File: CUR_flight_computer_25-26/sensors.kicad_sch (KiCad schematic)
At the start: 25 parts, among them U2 IIS2MDC, U3 LPS22HB, U4 LSM6DSV80X

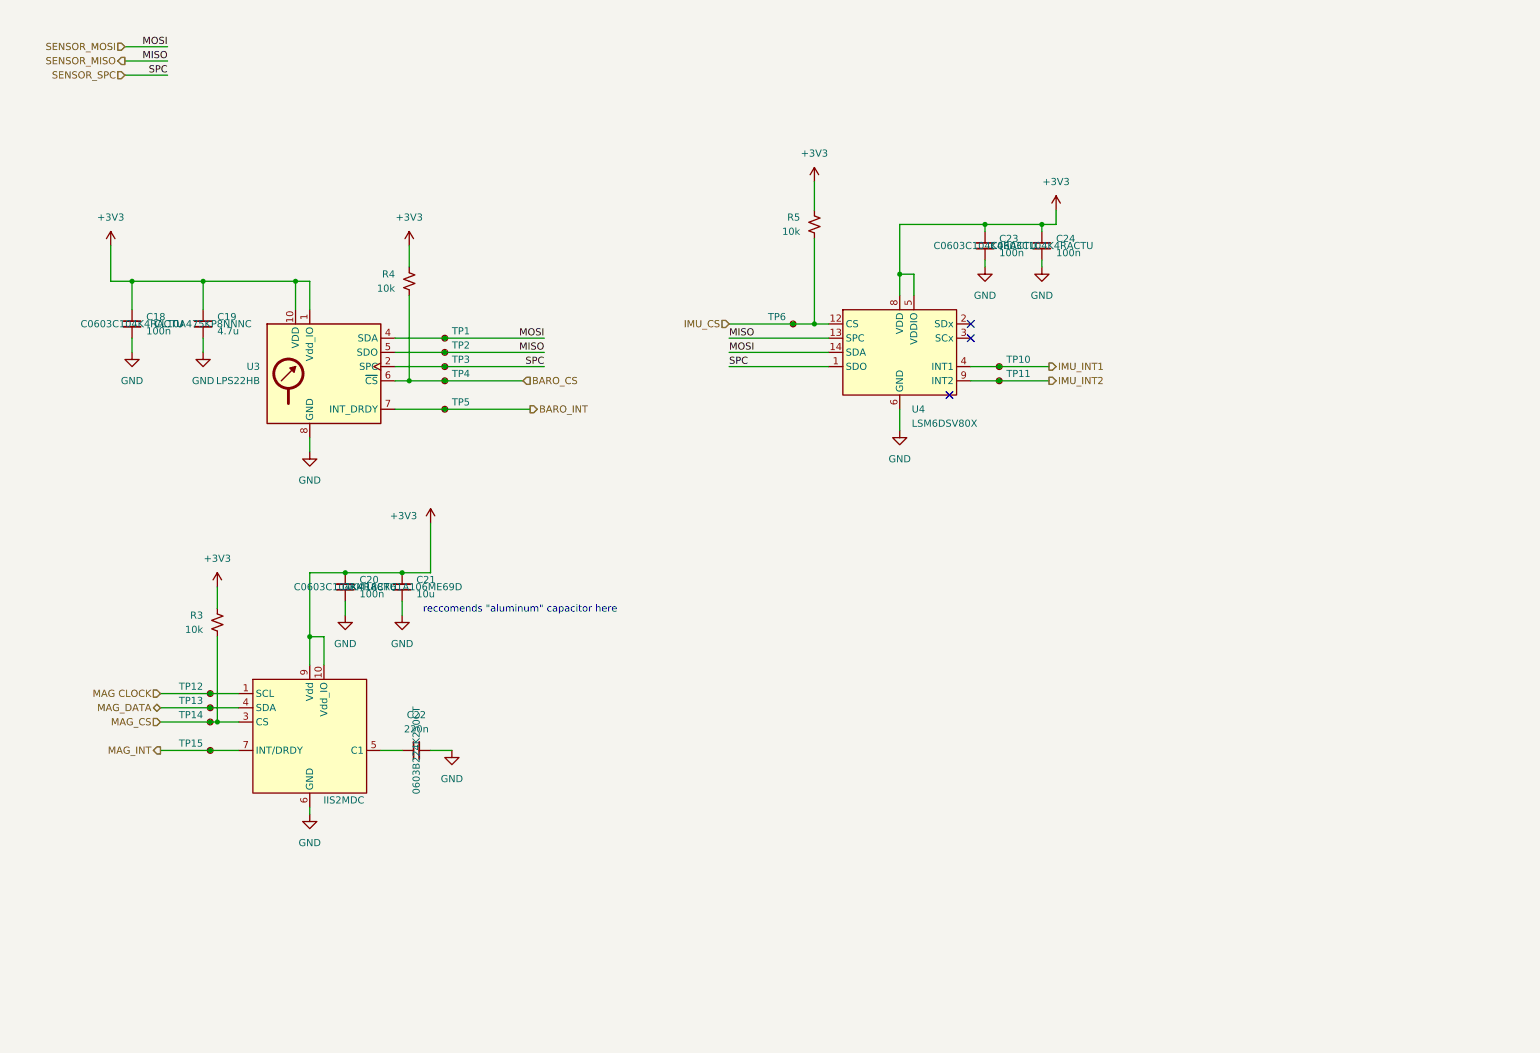
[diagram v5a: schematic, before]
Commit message: Add MPNs for ICs
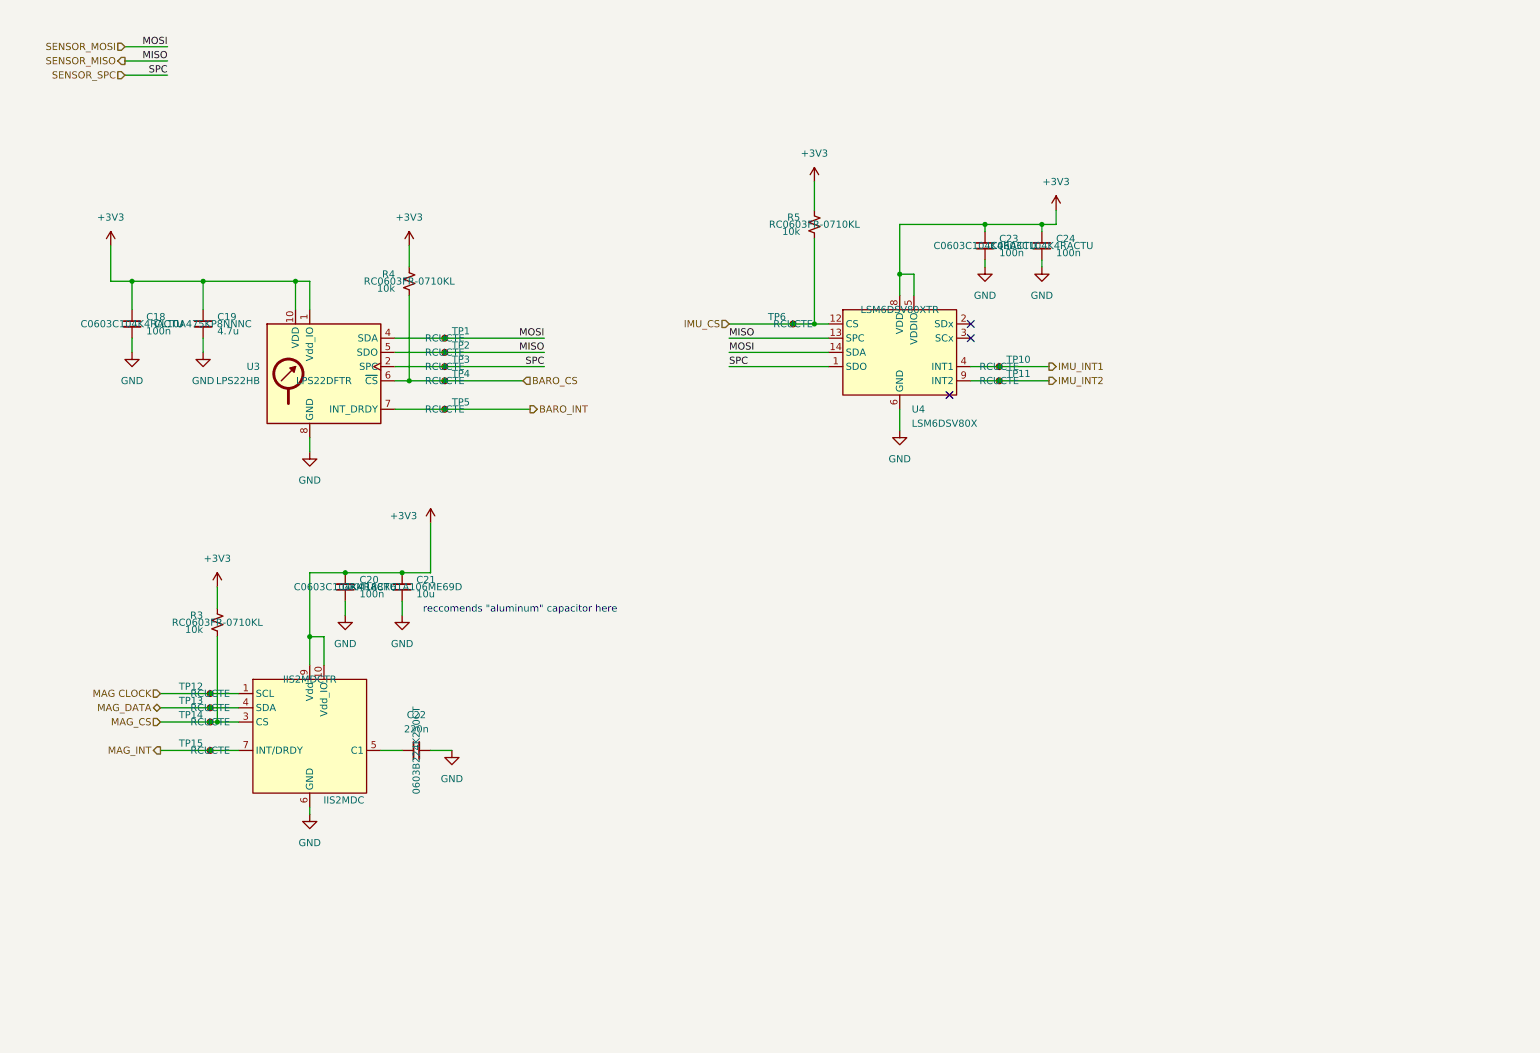
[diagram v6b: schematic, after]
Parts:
- R3, R4, R5: MPN (none) -> RC0603FR-0710KL
- TP1, TP10, TP11, TP12, TP13, TP14, TP15, TP2, TP3, TP4, TP5, TP6: value TestPoint_Small -> RCUCTE; MPN (none) -> RCUCTE
- U2: MPN (none) -> IIS2MDCTR
- U3: MPN (none) -> LPS22DFTR
- U4: MPN (none) -> LSM6DSV80XTR
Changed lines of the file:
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@@
+			)
+		)
+		(property "MPN" "RC0603FR-0710KL"
+			(at 156.21 50.8 0)
+			(effects
+				(font
+					(size 1.27 1.27)
+				)
 			)
 		)
@@
 			)
 		)
-		(property "Value" "TestPoint_Small"
+		(property "Value" "RCUCTE"
 			(at 91.44 77.4699 0)
 			(effects
@@
 				)
 				(hide yes)
+			)
+		)
+		(property "MPN" "RCUCTE"
+			(at 90.17 76.2 0)
+			(effects
+				(font
+					(size 1.27 1.27)
+				)
 			)
 		)
@@
 			)
 		)
-		(property "Value" "TestPoint_Small"
+		(property "Value" "RCUCTE"
 			(at 153.162 65.024 0)
 			(effects
@@
 			)
 		)
+		(property "MPN" "RCUCTE"
+			(at 152.4 68.58 0)
+			(effects
+				(font
+					(size 1.27 1.27)
+				)
+			)
+		)
 		(pin "1"
 		)
@@
 			)
 		)
+		(property "MPN" "LPS22DFTR"
+			(at 68.58 78.74 0)
+			(effects
+				(font
+					(size 1.27 1.27)
+				)
+			)
+		)
 		(pin "7"
 		)
@@
 			)
 		)
+		(property "MPN" "RC0603FR-0710KL"
+			(at 83.82 60.96 0)
+			(effects
+				(font
+					(size 1.27 1.27)
+				)
+			)
+		)
 		(pin "1"
 		)
@@
 			)
 		)
-		(property "Value" "TestPoint_Small"
+		(property "Value" "RCUCTE"
 			(at 89.408 67.564 0)
 			(effects
@@
 			)
 		)
+		(property "MPN" "RCUCTE"
+			(at 90.17 71.12 0)
+			(effects
+				(font
+					(size 1.27 1.27)
+				)
+			)
+		)
 		(pin "1"
 		)
@@
 			)
 		)
+		(property "MPN" "LSM6DSV80XTR"
+			(at 171.45 66.04 0)
+			(effects
+				(font
+					(size 1.27 1.27)
+				)
+			)
+		)
 		(pin "7"
 		)
@@
 			)
 		)
-		(property "Value" "TestPoint_Small"
+		(property "Value" "RCUCTE"
 			(at 91.44 74.9299 0)
 			(effects
@@
 			)
 		)
+		(property "MPN" "RCUCTE"
+			(at 90.17 73.66 0)
+			(effects
+				(font
+					(size 1.27 1.27)
+				)
+			)
+		)
 		(pin "1"
 		)
@@
 			)
 		)
-		(property "Value" "TestPoint_Small"
+		(property "Value" "RCUCTE"
 			(at 91.44 85.0899 0)
 			(effects
@@
 				)
 				(hide yes)
+			)
+		)
+		(property "MPN" "RCUCTE"
+			(at 90.17 83.82 0)
+			(effects
+				(font
+					(size 1.27 1.27)
+				)
 			)
 		)
@@
 			)
 		)
-		(property "Value" "TestPoint_Small"
+		(property "Value" "RCUCTE"
 			(at 46.99 146.0499 0)
 			(effects
@@
 			)
 		)
+		(property "MPN" "RCUCTE"
+			(at 48.26 144.78 0)
+			(effects
+				(font
+					(size 1.27 1.27)
+				)
+			)
+		)
 		(pin "1"
 		)
@@
 			)
 		)
+		(property "MPN" "IIS2MDCTR"
+			(at 66.04 132.08 0)
+			(effects
+				(font
+					(size 1.27 1.27)
+				)
+			)
+		)
 		(pin "4"
 		)
@@
 			)
 		)
-		(property "Value" "TestPoint_Small"
+		(property "Value" "RCUCTE"
 			(at 190.5 80.0099 0)
 			(effects
@@
 				)
 				(hide yes)
+			)
+		)
+		(property "MPN" "RCUCTE"
+			(at 189.23 78.74 0)
+			(effects
+				(font
+					(size 1.27 1.27)
+				)
 			)
 		)
@@
 			)
 		)
-		(property "Value" "TestPoint_Small"
+		(property "Value" "RCUCTE"
 			(at 49.022 131.064 0)
 			(effects
@@
 			)
 		)
+		(property "MPN" "RCUCTE"
+			(at 48.26 134.62 0)
+			(effects
+				(font
+					(size 1.27 1.27)
+				)
+			)
+		)
 		(pin "1"
 		)
@@
 				)
 				(hide yes)
+			)
+		)
+		(property "MPN" "RC0603FR-0710KL"
+			(at 49.53 121.92 0)
+			(effects
+				(font
+					(size 1.27 1.27)
+				)
 			)
 		)
@@
 			)
 		)
-		(property "Value" "TestPoint_Small"
+		(property "Value" "RCUCTE"
 			(at 46.99 138.4299 0)
 			(effects
@@
 			)
 		)
+		(property "MPN" "RCUCTE"
+			(at 48.26 137.16 0)
+			(effects
+				(font
+					(size 1.27 1.27)
+				)
+			)
+		)
 		(pin "1"
 		)
@@
 			)
 		)
-		(property "Value" "TestPoint_Small"
+		(property "Value" "RCUCTE"
 			(at 188.468 72.644 0)
 			(effects
@@
 			)
 		)
+		(property "MPN" "RCUCTE"
+			(at 189.23 76.2 0)
+			(effects
+				(font
+					(size 1.27 1.27)
+				)
+			)
+		)
 		(pin "1"
 		)
@@
 			)
 		)
-		(property "Value" "TestPoint_Small"
+		(property "Value" "RCUCTE"
 			(at 91.44 80.0099 0)
 			(effects
@@
 				)
 				(hide yes)
+			)
+		)
+		(property "MPN" "RCUCTE"
+			(at 90.17 78.74 0)
+			(effects
+				(font
+					(size 1.27 1.27)
+				)
 			)
 		)
@@
 			)
 		)
-		(property "Value" "TestPoint_Small"
+		(property "Value" "RCUCTE"
 			(at 46.99 140.9699 0)
 			(effects
@@
 			)
 		)
+		(property "MPN" "RCUCTE"
+			(at 48.26 139.7 0)
+			(effects
+				(font
+					(size 1.27 1.27)
+				)
+			)
+		)

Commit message: Hide MPNs
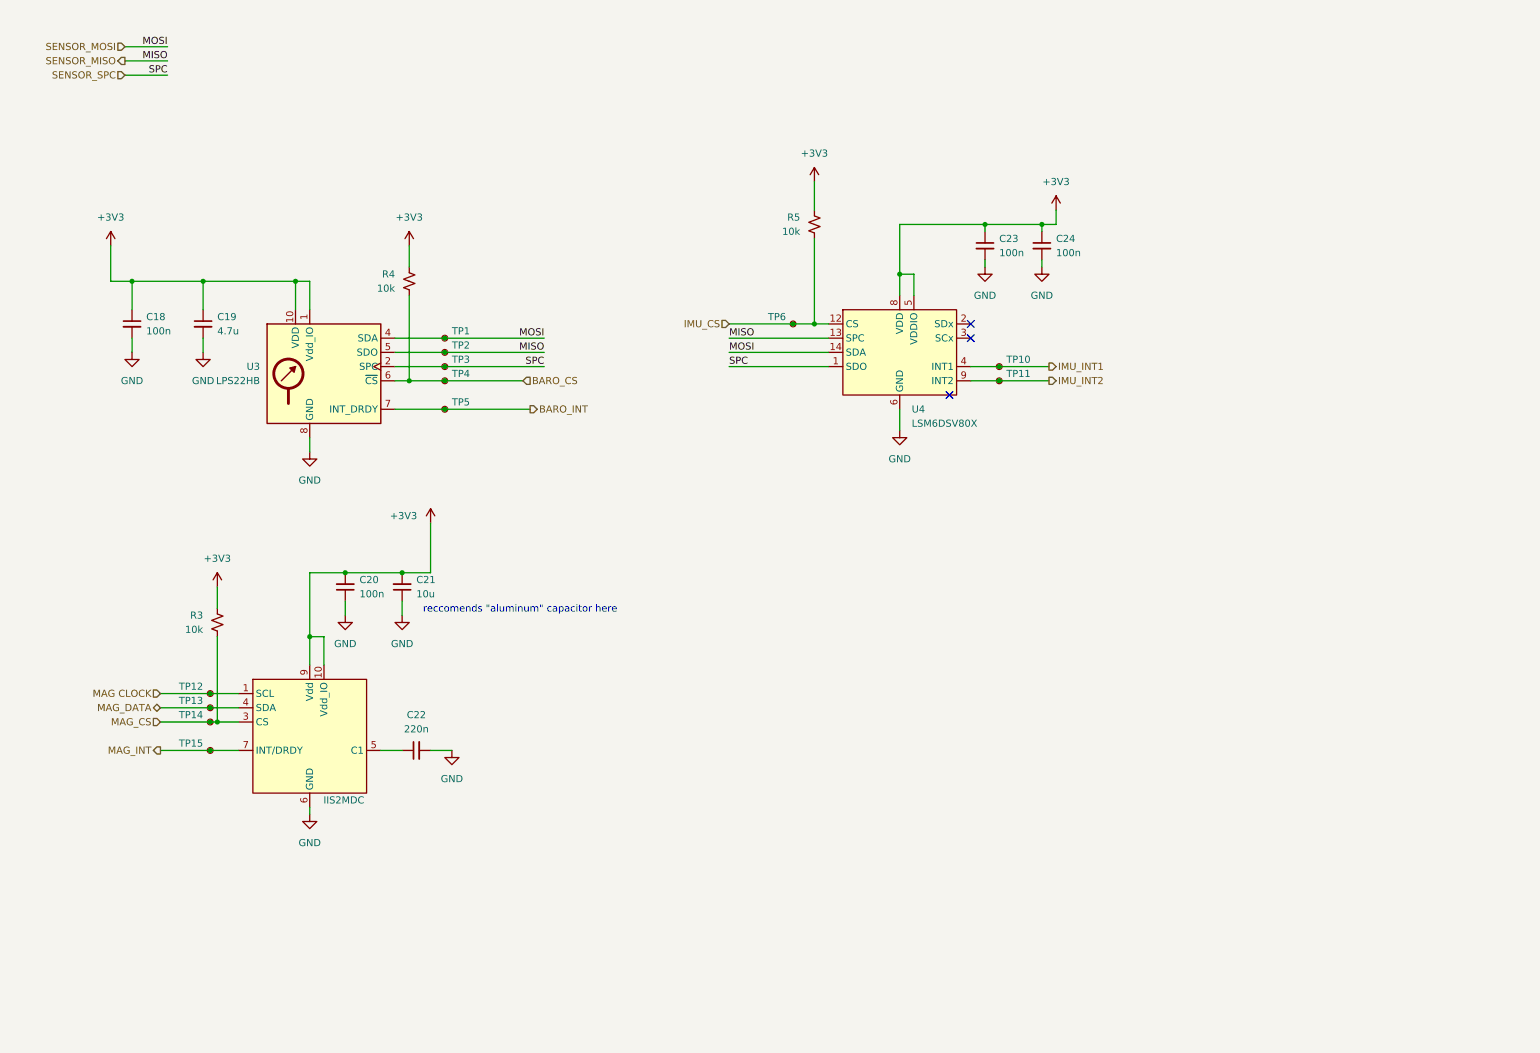
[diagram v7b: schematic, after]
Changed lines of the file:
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@@
 					(size 1.27 1.27)
 				)
+				(hide yes)
 			)
 		)
@@
 					(size 1.27 1.27)
 				)
+				(hide yes)
 			)
 		)
@@
 					(size 1.27 1.27)
 				)
+				(hide yes)
 			)
 		)
@@
 					(size 1.27 1.27)
 				)
+				(hide yes)
 			)
 		)
@@
 					(size 1.27 1.27)
 				)
+				(hide yes)
 			)
 		)
@@
 					(size 1.27 1.27)
 				)
+				(hide yes)
 			)
 		)
@@
 					(size 1.27 1.27)
 				)
+				(hide yes)
 			)
 		)
@@
 					(size 1.27 1.27)
 				)
+				(hide yes)
 			)
 		)
@@
 					(size 1.27 1.27)
 				)
+				(hide yes)
 			)
 		)
@@
 					(size 1.27 1.27)
 				)
+				(hide yes)
 			)
 		)
@@
 					(size 1.27 1.27)
 				)
+				(hide yes)
 			)
 		)
@@
 					(size 1.27 1.27)
 				)
+				(hide yes)
 			)
 		)
@@
 					(size 1.27 1.27)
 				)
+				(hide yes)
 			)
 		)
@@
 					(size 1.27 1.27)
 				)
+				(hide yes)
 			)
 		)
@@
 					(size 1.27 1.27)
 				)
+				(hide yes)
 			)
 		)
@@
 					(size 1.27 1.27)
 				)
+				(hide yes)
 			)
 		)
@@
 					(size 1.27 1.27)
 				)
+				(hide yes)
 			)
 		)
@@
 					(size 1.27 1.27)
 				)
+				(hide yes)
 			)
 		)
@@
 					(size 1.27 1.27)
 				)
+				(hide yes)
 			)
 		)
@@
 					(size 1.27 1.27)
 				)
+				(hide yes)
 			)
 		)
@@
 					(size 1.27 1.27)
 				)
+				(hide yes)
 			)
 		)
@@
 					(size 1.27 1.27)
 				)
+				(hide yes)
 			)
 		)
@@
 					(size 1.27 1.27)
 				)
+				(hide yes)
 			)
 		)
@@
 					(size 1.27 1.27)
 				)
+				(hide yes)
 			)
 		)
@@
 					(size 1.27 1.27)
 				)
-			)
-		)
+				(hide yes)
+			)
+		)

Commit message: Cleaned up schematic
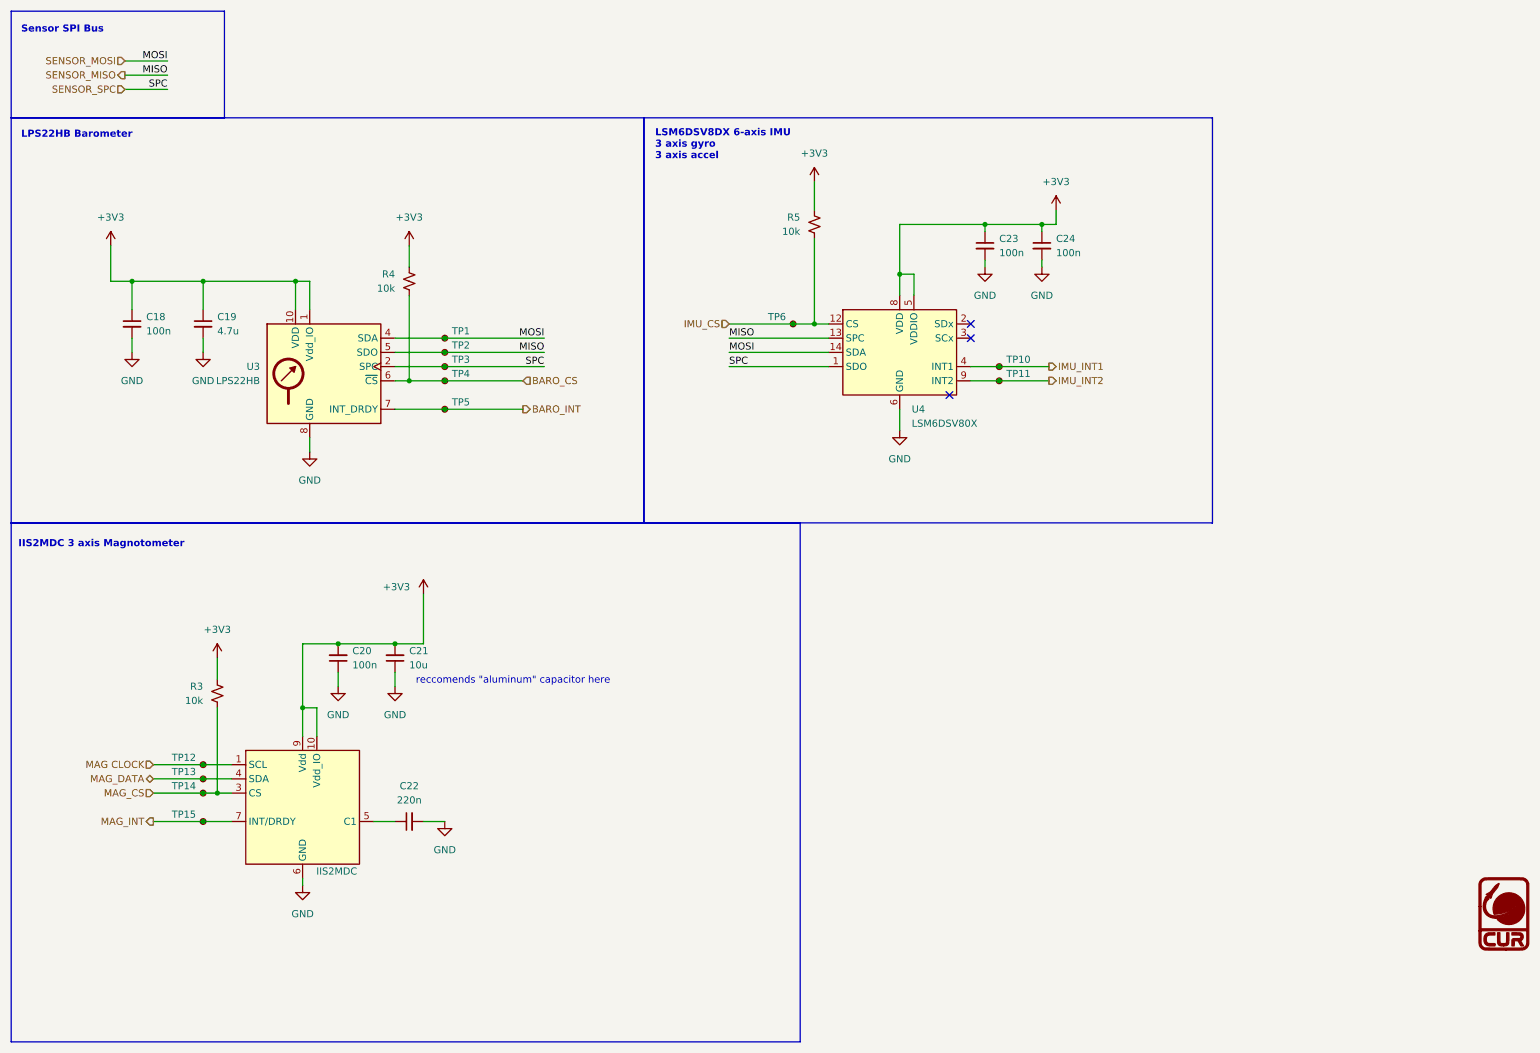
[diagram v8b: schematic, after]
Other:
- note added: "IIS2MDC 3 axis Magnotometer"
- note added: "LPS22HB Barometer"
- note added: "LSM6DSV8DX 6-axis IMU 3 axis gyro 3 axis accel"
- note added: "Sensor SPI Bus"
- company: (none) -> Clarkson University Rocketry
- title: (none) -> Flight Computer
- moved on the sheet: C20, C21, C22, R3, TP12, TP13, TP14, TP15
